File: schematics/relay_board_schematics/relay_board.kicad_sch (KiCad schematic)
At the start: 45 parts, among them J1 Programming Header, P1 ACT_PWR, P2 ACT_PWR, P3 ACTUATOR, Q1 MMBF170, Q2 MMBF170, SW1 SW_DIP_x04, U1 SPST_POWER_RELAY, U2 PIC16F1826-ISO, U3 dpdt_relay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

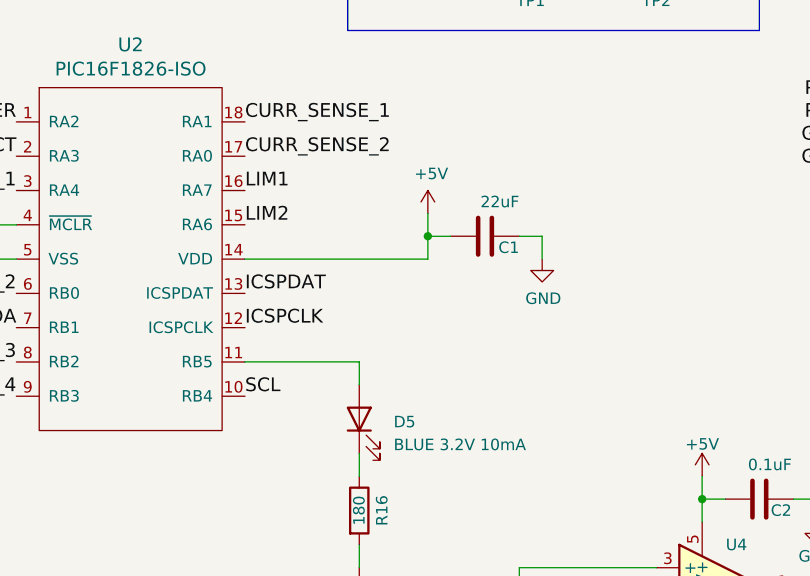
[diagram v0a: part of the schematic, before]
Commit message: added missing decoupling cap to PIC VDD, moved decoupling caps closer to ICs, fixed main power connections, small tweaks to trace routing
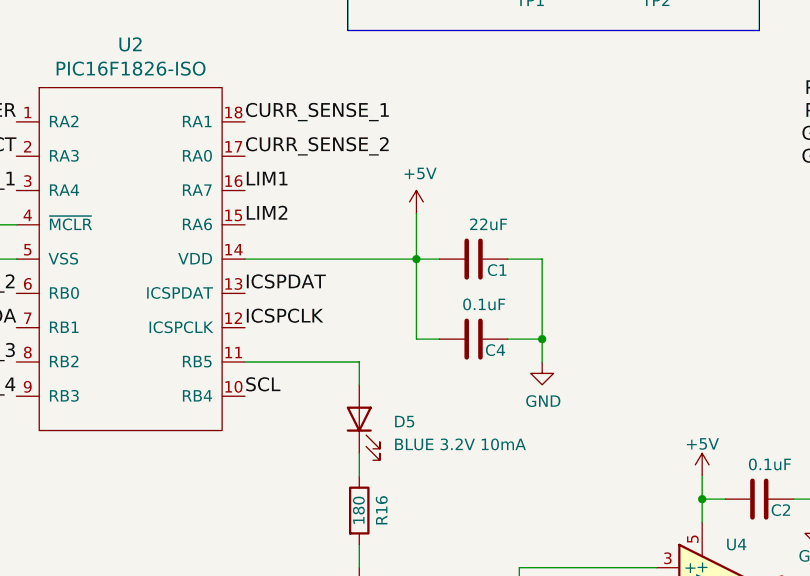
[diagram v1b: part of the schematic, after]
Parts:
- added C4: 0.1uF, Capacitor_SMD:C_0805_2012Metric_Pad1.18x1.45mm_HandSolder, symbol relay_board:C-rlcs_relay_board
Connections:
- net +5V: now also C4.2
- net GND: now also C4.1
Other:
- moved on the sheet: C1
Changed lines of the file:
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@@
   (junction (at 261.62 69.85) (diameter 0) (color 0 0 0 0)
   )
+  (junction (at 204.47 72.39) (diameter 0) (color 0 0 0 0)
+  )
   (junction (at 158.75 110.49) (diameter 0) (color 0 0 0 0)
   )
+  (junction (at 190.5 63.5) (diameter 0) (color 0 0 0 0)
+  )
   (junction (at 217.17 26.67) (diameter 0) (color 0 0 0 0)
   )
-  (junction (at 191.77 60.96) (diameter 0) (color 0 0 0 0)
-  )
   (junction (at 105.41 39.37) (diameter 0) (color 0 0 0 0)
   )
@@
     (stroke (width 0) (type default) (color 0 0 0 0))
   )
-  (wire (pts (xy 201.93 60.96) (xy 204.47 60.96))
-    (stroke (width 0) (type default) (color 0 0 0 0))
-  )
   (wire (pts (xy 184.15 74.93) (xy 171.45 74.93))
     (stroke (width 0) (type default) (color 0 0 0 0))
@@
     (stroke (width 0) (type default) (color 0 0 0 0))
   )
+  (wire (pts (xy 204.47 72.39) (xy 204.47 74.93))
+    (stroke (width 0) (type default) (color 0 0 0 0))
+  )
   (wire (pts (xy 116.84 173.99) (xy 119.38 173.99))
     (stroke (width 0) (type default) (color 0 0 0 0))
@@
     (stroke (width 0) (type default) (color 0 0 0 0))
   )
-  (wire (pts (xy 191.77 60.96) (xy 194.31 60.96))
-    (stroke (width 0) (type default) (color 0 0 0 0))
-  )
   (wire (pts (xy 100.33 114.3) (xy 104.14 114.3))
     (stroke (width 0) (type default) (color 0 0 0 0))
@@
     (stroke (width 0) (type default) (color 0 0 0 0))
   )
+  (wire (pts (xy 204.47 63.5) (xy 204.47 72.39))
+    (stroke (width 0) (type default) (color 0 0 0 0))
+  )
   (wire (pts (xy 137.16 121.92) (xy 134.62 121.92))
     (stroke (width 0) (type default) (color 0 0 0 0))
   )
+  (wire (pts (xy 190.5 63.5) (xy 193.04 63.5))
+    (stroke (width 0) (type default) (color 0 0 0 0))
+  )
   (wire (pts (xy 129.54 165.1) (xy 129.54 167.64))
     (stroke (width 0) (type default) (color 0 0 0 0))
@@
     (stroke (width 0) (type default) (color 0 0 0 0))
   )
+  (wire (pts (xy 204.47 72.39) (xy 200.66 72.39))
+    (stroke (width 0) (type default) (color 0 0 0 0))
+  )
   (wire (pts (xy 162.56 162.56) (xy 162.56 165.1))
     (stroke (width 0) (type default) (color 0 0 0 0))
@@
     (stroke (width 0) (type default) (color 0 0 0 0))
   )
-  (wire (pts (xy 191.77 60.96) (xy 191.77 63.5))
-    (stroke (width 0) (type default) (color 0 0 0 0))
-  )
   (wire (pts (xy 222.25 25.4) (xy 222.25 26.67))
     (stroke (width 0) (type default) (color 0 0 0 0))
@@
     (stroke (width 0) (type default) (color 0 0 0 0))
   )
-  (wire (pts (xy 204.47 60.96) (xy 204.47 63.5))
-    (stroke (width 0) (type default) (color 0 0 0 0))
-  )
   (wire (pts (xy 38.1 69.85) (xy 38.1 68.58))
     (stroke (width 0) (type default) (color 0 0 0 0))
@@
     (stroke (width 0) (type default) (color 0 0 0 0))
   )
+  (wire (pts (xy 190.5 63.5) (xy 190.5 72.39))
+    (stroke (width 0) (type default) (color 0 0 0 0))
+  )
   (wire (pts (xy 87.63 44.45) (xy 105.41 44.45))
     (stroke (width 0) (type default) (color 0 0 0 0))
@@
     (stroke (width 0) (type default) (color 0 0 0 0))
   )
+  (wire (pts (xy 190.5 58.42) (xy 190.5 63.5))
+    (stroke (width 0) (type default) (color 0 0 0 0))
+  )
   (wire (pts (xy 261.62 58.42) (xy 261.62 59.69))
     (stroke (width 0) (type default) (color 0 0 0 0))
   )
-  (wire (pts (xy 191.77 58.42) (xy 191.77 60.96))
+  (wire (pts (xy 200.66 63.5) (xy 204.47 63.5))
     (stroke (width 0) (type default) (color 0 0 0 0))
   )
@@
     (stroke (width 0) (type default) (color 0 0 0 0))
   )
-  (wire (pts (xy 171.45 63.5) (xy 191.77 63.5))
+  (wire (pts (xy 171.45 63.5) (xy 190.5 63.5))
     (stroke (width 0) (type default) (color 0 0 0 0))
   )
@@
   )
   (wire (pts (xy 87.63 52.07) (xy 97.79 52.07))
+    (stroke (width 0) (type default) (color 0 0 0 0))
+  )
+  (wire (pts (xy 190.5 72.39) (xy 193.04 72.39))
     (stroke (width 0) (type default) (color 0 0 0 0))
   )
@@
     (pin "9")
   )
-  (symbol (lib_id "power:+5V") (at 191.77 58.42 0) (unit 1)
-    (in_bom yes) (on_board yes)
-    (property "Reference" "#PWR026" (id 0) (at 191.77 62.23 0)
-      (effects (font (size 1.27 1.27)) hide)
-    )
-    (property "Value" "+5V" (id 1) (at 192.151 54.0258 0))
-    (property "Footprint" "" (id 2) (at 191.77 58.42 0)
-      (effects (font (size 1.27 1.27)) hide)
-    )
-    (property "Datasheet" "" (id 3) (at 191.77 58.42 0)
+  (symbol (lib_id "power:+5V") (at 190.5 58.42 0) (unit 1)
+    (in_bom yes) (on_board yes)
+    (property "Reference" "#PWR026" (id 0) (at 190.5 62.23 0)
+      (effects (font (size 1.27 1.27)) hide)
+    )
+    (property "Value" "+5V" (id 1) (at 190.881 54.0258 0))
+    (property "Footprint" "" (id 2) (at 190.5 58.42 0)
+      (effects (font (size 1.27 1.27)) hide)
+    )
+    (property "Datasheet" "" (id 3) (at 190.5 58.42 0)
       (effects (font (size 1.27 1.27)) hide)
     )
@@
     (pin "1")
   )
-  (symbol (lib_id "Device:C") (at 198.12 60.96 90) (unit 1)
-    (in_bom yes) (on_board yes)
-    (property "Reference" "C1" (id 0) (at 201.93 62.23 90)
-      (effects (font (size 1.27 1.27)) (justify left))
-    )
-    (property "Value" "22uF" (id 1) (at 201.93 57.15 90)
-      (effects (font (size 1.27 1.27)) (justify left))
-    )
-    (property "Footprint" "Capacitor_SMD:C_0805_2012Metric_Pad1.18x1.45mm_HandSolder" (id 2) (at 201.93 59.9948 0)
-      (effects (font (size 1.27 1.27)) hide)
-    )
-    (property "Datasheet" "~" (id 3) (at 198.12 60.96 0)
-      (effects (font (size 1.27 1.27)) hide)
-    )
-    (pin "1")
-    (pin "2")
-  )
-  (symbol (lib_id "relay_board:GND-rlcs_relay_board") (at 204.47 63.5 0) (unit 1)
-    (in_bom yes) (on_board yes)
-    (property "Reference" "#PWR027" (id 0) (at 204.47 69.85 0)
-      (effects (font (size 1.27 1.27)) hide)
-    )
-    (property "Value" "GND" (id 1) (at 204.597 67.8942 0))
-    (property "Footprint" "" (id 2) (at 204.47 63.5 0)
-      (effects (font (size 1.27 1.27)) hide)
-    )
-    (property "Datasheet" "" (id 3) (at 204.47 63.5 0)
+  (symbol (lib_id "Device:C") (at 196.85 63.5 90) (unit 1)
+    (in_bom yes) (on_board yes)
+    (property "Reference" "C1" (id 0) (at 200.66 64.77 90)
+      (effects (font (size 1.27 1.27)) (justify left))
+    )
+    (property "Value" "22uF" (id 1) (at 200.66 59.69 90)
+      (effects (font (size 1.27 1.27)) (justify left))
+    )
+    (property "Footprint" "Capacitor_SMD:C_0805_2012Metric_Pad1.18x1.45mm_HandSolder" (id 2) (at 200.66 62.5348 0)
+      (effects (font (size 1.27 1.27)) hide)
+    )
+    (property "Datasheet" "~" (id 3) (at 196.85 63.5 0)
+      (effects (font (size 1.27 1.27)) hide)
+    )
+    (pin "1")
+    (pin "2")
+  )
+  (symbol (lib_id "relay_board:GND-rlcs_relay_board") (at 204.47 74.93 0) (unit 1)
+    (in_bom yes) (on_board yes)
+    (property "Reference" "#PWR027" (id 0) (at 204.47 81.28 0)
+      (effects (font (size 1.27 1.27)) hide)
+    )
+    (property "Value" "GND" (id 1) (at 204.597 79.3242 0))
+    (property "Footprint" "" (id 2) (at 204.47 74.93 0)
+      (effects (font (size 1.27 1.27)) hide)
+    )
+    (property "Datasheet" "" (id 3) (at 204.47 74.93 0)
       (effects (font (size 1.27 1.27)) hide)
     )
@@
     (pin "1")
   )
+  (symbol (lib_id "relay_board:C-rlcs_relay_board") (at 196.85 72.39 270) (unit 1)
+    (in_bom yes) (on_board yes)
+    (property "Reference" "C4" (id 0) (at 198.12 73.66 90)
+      (effects (font (size 1.27 1.27)) (justify left))
+    )
+    (property "Value" "0.1uF" (id 1) (at 195.58 68.58 90)
+      (effects (font (size 1.27 1.27)) (justify left))
+    )
+    (property "Footprint" "Capacitor_SMD:C_0805_2012Metric_Pad1.18x1.45mm_HandSolder" (id 2) (at 193.04 73.3552 0)
+      (effects (font (size 1.27 1.27)) hide)
+    )
+    (property "Datasheet" "" (id 3) (at 196.85 72.39 0)
+      (effects (font (size 1.27 1.27)) hide)
+    )
+    (pin "1")
+    (pin "2")
+  )
   (symbol (lib_id "power:PWR_FLAG") (at 208.28 25.4 0) (unit 1)
     (in_bom yes) (on_board yes)
@@
       (reference "C3") (unit 1) (value "0.1uF") (footprint "Capacitor_SMD:C_0805_2012Metric_Pad1.18x1.45mm_HandSolder")
     )
+    (path "/2fd59d0c-2840-4aeb-8f74-5c3ab86ddc9e"
+      (reference "C4") (unit 1) (value "0.1uF") (footprint "Capacitor_SMD:C_0805_2012Metric_Pad1.18x1.45mm_HandSolder")
+    )
     (path "/00000000-0000-0000-0000-00005dfd5087"
